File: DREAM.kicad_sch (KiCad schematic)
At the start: 0 parts

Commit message: feat: checked REV A
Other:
- sheet PROJECT ARCHITECTURE renamed ARCHITECTURE
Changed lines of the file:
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@@
 			(color 0 0 0 0.0000)
 		)
-		(property "Sheetname" "PROJECT ARCHITECTURE"
+		(property "Sheetname" "ARCHITECTURE"
 			(at 299.72 312.6609 0)
 			(effects

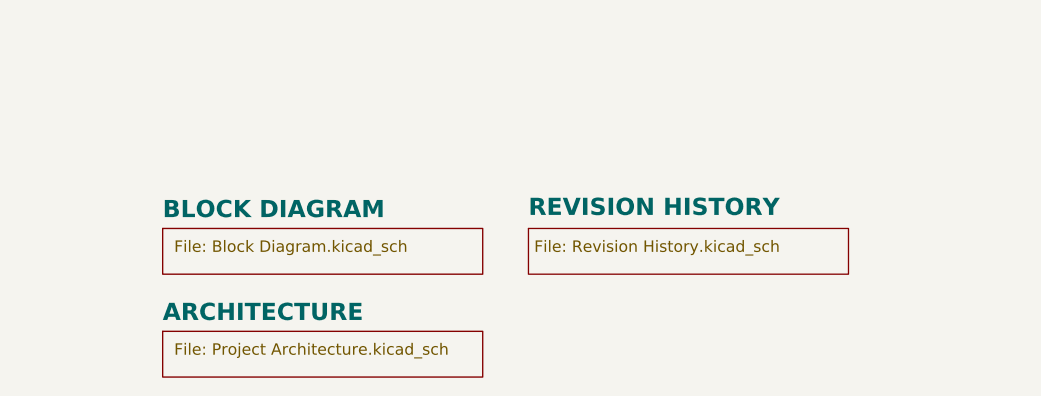
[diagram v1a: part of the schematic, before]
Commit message: fix: circuit schem as one sheet
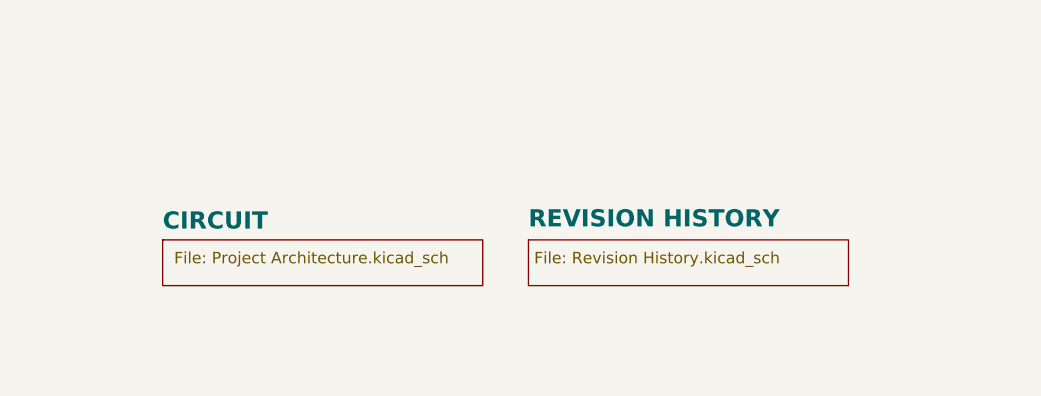
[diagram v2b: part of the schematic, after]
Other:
- sheet ARCHITECTURE renamed CIRCUIT
- removed sheet BLOCK DIAGRAM
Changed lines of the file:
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@@
 	(paper "A3")
 	(title_block
-		(date "2026-04-06")
+		(date "2026-05-09")
 		(rev "${REVISION}")
 		(company "${COMPANY}")
@@
 	)
 	(sheet
-		(at 340.36 302.26)
+		(at 340.36 303.53)
 		(size 35.56 5.08)
 		(exclude_from_sim no)
@@
 		)
 		(property "Sheetname" "REVISION HISTORY"
-			(at 340.36 300.99 0)
+			(at 340.36 302.26 0)
 			(effects
 				(font
@@
 		)
 		(property "Sheetfile" "Revision History.kicad_sch"
-			(at 340.995 303.53 0)
+			(at 340.995 304.8 0)
 			(effects
 				(font
@@
 			(project "DREAM"
 				(path "/f9e05184-c88b-4a88-ae9c-ab2bdb32be7c"
-					(page "8")
+					(page "3")
 				)
 			)
@@
 	)
 	(sheet
-		(at 299.72 302.26)
+		(at 299.72 303.53)
 		(size 35.56 5.08)
 		(exclude_from_sim no)
@@
 			(color 0 0 0 0.0000)
 		)
-		(property "Sheetname" "BLOCK DIAGRAM"
-			(at 299.72 301.2309 0)
+		(property "Sheetname" "CIRCUIT"
+			(at 299.72 302.5009 0)
 			(effects
 				(font
@@
 			)
 		)
-		(property "Sheetfile" "Block Diagram.kicad_sch"
-			(at 300.99 303.53 0)
+		(property "Sheetfile" "Project Architecture.kicad_sch"
+			(at 300.99 304.8 0)
 			(effects
 				(font
@@
 				)
 			)
-		)
-	)
-	(sheet
-		(at 299.72 313.69)
-		(size 35.56 5.08)
-		(exclude_from_sim no)
-		(in_bom yes)
-		(on_board yes)
-		(dnp no)
-		(stroke
-			(width 0.1524)
-			(type solid)
-		)
-		(fill
-			(color 0 0 0 0.0000)
-		)
-		(property "Sheetname" "ARCHITECTURE"
-			(at 299.72 312.6609 0)
-			(effects
-				(font
-					(face "Times New Roman")
-					(size 1.905 1.905)
-					(bold yes)
-					(color 0 0 0 1)
-				)
-				(justify left bottom)
-			)
-		)
-		(property "Sheetfile" "Project Architecture.kicad_sch"
-			(at 300.99 314.96 0)
-			(effects
-				(font
-					(face "Arial")
-					(size 1.27 1.27)
-				)
-				(justify left top)
-			)
-		)
-		(instances
-			(project "DREAM"
-				(path "/f9e05184-c88b-4a88-ae9c-ab2bdb32be7c"
-					(page "3")
-				)
-			)
